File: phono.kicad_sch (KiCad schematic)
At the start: 63 parts, among them J1 Power +30V, J2 R Phono in, J3 L Phono in, J4 R Phono out, J5 L Phono out, Q1 2N2222, Q2 2N2222, Q3 2N2222, Q4 2N2222, Q5 2N2222, Q6 2N2222

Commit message: Add files via upload
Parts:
- removed C1, C11, C12, C13, C14, C15, C16, C17, C2, C4, C8, C9: 150uf, Capacitor_THT:CP_Radial_D10.0mm_P5.00mm, symbol Device:C_Polarized
- removed C10, C5: 47uf, Capacitor_THT:CP_Radial_D6.3mm_P2.50mm, symbol Device:C_Polarized
- removed C18, C6: 15uf, Capacitor_THT:CP_Radial_D5.0mm_P2.00mm, symbol Device:C_Polarized
- removed C19, C21: 6.8nf, Capacitor_THT:C_Rect_L7.0mm_W2.0mm_P5.00mm, symbol Device:C
- removed C20, C22: 22nf, Capacitor_THT:C_Rect_L7.0mm_W2.0mm_P5.00mm, symbol Device:C
- removed C3, C7: 1uf, Capacitor_THT:CP_Radial_D4.0mm_P2.00mm, symbol Device:C_Polarized
- removed D1, D2: 1N5250B, Diode_THT:D_DO-41_SOD81_P10.16mm_Horizontal, symbol Diode:1N47xxA
- removed J1: Power +30V, Connector_Wire:SolderWire-2sqmm_1x02_P7.8mm_D2mm_OD3.9mm, symbol Connector:Conn_01x02_Pin
- removed J2: R Phono in, Connector_Wire:SolderWire-2sqmm_1x01_D2mm_OD3.9mm, symbol Connector:Conn_01x01_Pin
- removed J3: L Phono in, Connector_Wire:SolderWire-2sqmm_1x01_D2mm_OD3.9mm, symbol Connector:Conn_01x01_Pin
- removed J4: R Phono out, Connector_Wire:SolderWire-2sqmm_1x01_D2mm_OD3.9mm, symbol Connector:Conn_01x01_Pin
- removed J5: L Phono out, Connector_Wire:SolderWire-2sqmm_1x01_D2mm_OD3.9mm, symbol Connector:Conn_01x01_Pin
- removed Q1, Q2, Q3, Q4, Q5, Q6: 2N2222, Package_TO_SOT_THT:TO-18-3, symbol Transistor_BJT:BC107
- removed R1, R15, R25, R8: 100, Resistor_THT:R_Axial_DIN0207_L6.3mm_D2.5mm_P10.16mm_Horizontal, symbol Device:R
- removed R10, R22: 270k, Resistor_THT:R_Axial_DIN0207_L6.3mm_D2.5mm_P10.16mm_Horizontal, symbol Device:R
- removed R11, R24: 6k, Resistor_THT:R_Axial_DIN0207_L6.3mm_D2.5mm_P10.16mm_Horizontal, symbol Device:R
- removed R12, R23: 680, Resistor_THT:R_Axial_DIN0207_L6.3mm_D2.5mm_P10.16mm_Horizontal, symbol Device:R
- removed R13, R27: 4k7, Resistor_THT:R_Axial_DIN0207_L6.3mm_D2.5mm_P10.16mm_Horizontal, symbol Device:R
- removed R14, R28: 10k, Resistor_THT:R_Axial_DIN0207_L6.3mm_D2.5mm_P10.16mm_Horizontal, symbol Device:R
- removed R16, R2: 47k, Resistor_THT:R_Axial_DIN0207_L6.3mm_D2.5mm_P10.16mm_Horizontal, symbol Device:R
- removed R17, R6: 8k2, Resistor_THT:R_Axial_DIN0207_L6.3mm_D2.5mm_P10.16mm_Horizontal, symbol Device:R
- removed R18, R3: 150, Resistor_THT:R_Axial_DIN0207_L6.3mm_D2.5mm_P10.16mm_Horizontal, symbol Device:R
- removed R19, R26, R4, R7: 1k8, Resistor_THT:R_Axial_DIN0207_L6.3mm_D2.5mm_P10.16mm_Horizontal, symbol Device:R
- removed R20, R5: 1k, Resistor_THT:R_Axial_DIN0207_L6.3mm_D2.5mm_P10.16mm_Horizontal, symbol Device:R
- removed R21, R9: 12k, Resistor_THT:R_Axial_DIN0207_L6.3mm_D2.5mm_P10.16mm_Horizontal, symbol Device:R
- added C1, C101, C102, C2, C8, C9: 300u, Capacitor_THT:CP_Radial_D10.0mm_P5.00mm, symbol Device:C_Polarized_Small
- added C103, C3: 6n8, Capacitor_THT:C_Axial_L3.8mm_D2.6mm_P10.00mm_Horizontal, symbol Device:C
- added C104, C4: 22n, Capacitor_THT:C_Axial_L3.8mm_D2.6mm_P10.00mm_Horizontal, symbol Device:C
- added C105, C5, C7: 47u, Capacitor_THT:CP_Radial_D10.0mm_P5.00mm, symbol Device:C_Polarized_Small
- added C106, C6: 1uF, Capacitor_THT:C_Axial_L3.8mm_D2.6mm_P10.00mm_Horizontal, symbol Device:C
- added J1, J3: Conn_01x03_Pin, TerminalBlock:TerminalBlock_bornier-3_P5.08mm, symbol Connector:Conn_01x03_Pin
- added J2: Conn_01x02_Pin, TerminalBlock:TerminalBlock_bornier-2_P5.08mm, symbol Connector:Conn_01x02_Pin
- added Q1, Q101, Q102, Q103, Q2, Q3: 2N2222, Package_TO_SOT_THT:TO-39-3, symbol Transistor_BJT:2N2219
- added R1, R101: 150, Resistor_THT:R_Axial_DIN0207_L6.3mm_D2.5mm_P10.16mm_Horizontal, symbol Device:R_Small
- added R10, R11, R110: 1K, Resistor_THT:R_Axial_DIN0207_L6.3mm_D2.5mm_P10.16mm_Horizontal, symbol Device:R_Small
- added R102, R109, R2, R9: 1K8, Resistor_THT:R_Axial_DIN0207_L6.3mm_D2.5mm_P10.16mm_Horizontal, symbol Device:R_Small
- added R103, R3: 8K2, Resistor_THT:R_Axial_DIN0207_L6.3mm_D2.5mm_P10.16mm_Horizontal, symbol Device:R_Small
- added R104, R108, R4, R8: 100, Resistor_THT:R_Axial_DIN0207_L6.3mm_D2.5mm_P10.16mm_Horizontal, symbol Device:R_Small
- added R105, R5: 12K, Resistor_THT:R_Axial_DIN0207_L6.3mm_D2.5mm_P10.16mm_Horizontal, symbol Device:R_Small
- added R106, R6: 270K, Resistor_THT:R_Axial_DIN0207_L6.3mm_D2.5mm_P10.16mm_Horizontal, symbol Device:R_Small
- added R107, R7: 6K, Resistor_THT:R_Axial_DIN0207_L6.3mm_D2.5mm_P10.16mm_Horizontal, symbol Device:R_Small
- added R112, R12: 47K, Resistor_THT:R_Axial_DIN0207_L6.3mm_D2.5mm_P10.16mm_Horizontal, symbol Device:R_Small
- added R113, R13: 4K7, Resistor_THT:R_Axial_DIN0207_L6.3mm_D2.5mm_P10.16mm_Horizontal, symbol Device:R_Small
- added R114, R14: 10K, Resistor_THT:R_Axial_DIN0207_L6.3mm_D2.5mm_P10.16mm_Horizontal, symbol Device:R_Small
- added R15: 15K, Resistor_THT:R_Axial_DIN0207_L6.3mm_D2.5mm_P10.16mm_Horizontal, symbol Device:R_Small
- added U1: LM317_TO-220, Package_TO_SOT_THT:TO-220-3_Vertical, symbol Regulator_Linear:LM317_TO-220
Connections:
- net +28V: now also J2.1 (Pin_1), Q103.3 (C), Q3.3 (C), R107.1, R7.2, U1.3 (VI)
- net GND: now also C1.2, C101.2, C102.2, C2.2, C7.2, C8.2, C9.2, J1.2 (Pin_2), J2.2 (Pin_2), J3.2 (Pin_2), R102.2, R109.2, R113.2, R114.2, R13.2, R14.2, R15.2, R2.2, R9.2
- new net: C106.2, R104.1
- new net: Q101.2 (B), R104.2, R112.1
- new net: C1.1, R1.2, R2.1
- new net: Q2.1 (E), R8.1
- new net: Q1.3 (C), Q2.2 (B), R3.2
- new net: C4.2, Q2.3 (C), Q3.2 (B), R6.2, R7.1
- new net: R11.2, R15.1, U1.1 (ADJ)
- new net: C2.1, R10.1, R12.2
- new net: C8.1, R10.2, R8.2, R9.1
- new net: C3.1, Q1.1 (E), R1.1, R5.1
- new net: C3.2, C4.1, R5.2, R6.1
- new net: C103.2, C104.1, R105.2, R106.1
- new net: C104.2, Q102.3 (C), Q103.2 (B), R106.2, R107.2
- new net: C105.1, Q103.1 (E), R113.1
- new net: C5.1, Q3.1 (E), R13.1
- new net: C6.2, R4.1
- new net: C103.1, Q101.1 (E), R101.1, R105.1
- new net: Q101.3 (C), Q102.2 (B), R103.2
- new net: C101.1, R101.2, R102.1
- new net: Q1.2 (B), R12.1, R4.2
- new net: C102.1, R110.1, R112.2
- new net: C9.1, R108.2, R109.1, R110.2
- new net: Q102.1 (E), R108.1
- new net +20V: C7.1, R103.1, R11.1, R3.1, U1.2 (VO)
- new net Input-L: C106.1, J1.3 (Pin_3)
- new net Input-R: C6.1, J1.1 (Pin_1)
- new net Output-L: C105.2, J3.3 (Pin_3), R114.1
- new net Output-R: C5.2, J3.1 (Pin_1), R14.1

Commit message: Add files via upload
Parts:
- added C10: 10u, Capacitor_THT:CP_Radial_D5.0mm_P2.00mm, symbol Device:C_Polarized_Small
- R11: value 1K -> 220
- R15: value 15K -> 3K3
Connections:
- net GND: now also C10.2
- net at R11.2, R15.1, U1.1 (ADJ): now also C10.1
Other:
- moved on the sheet: R15

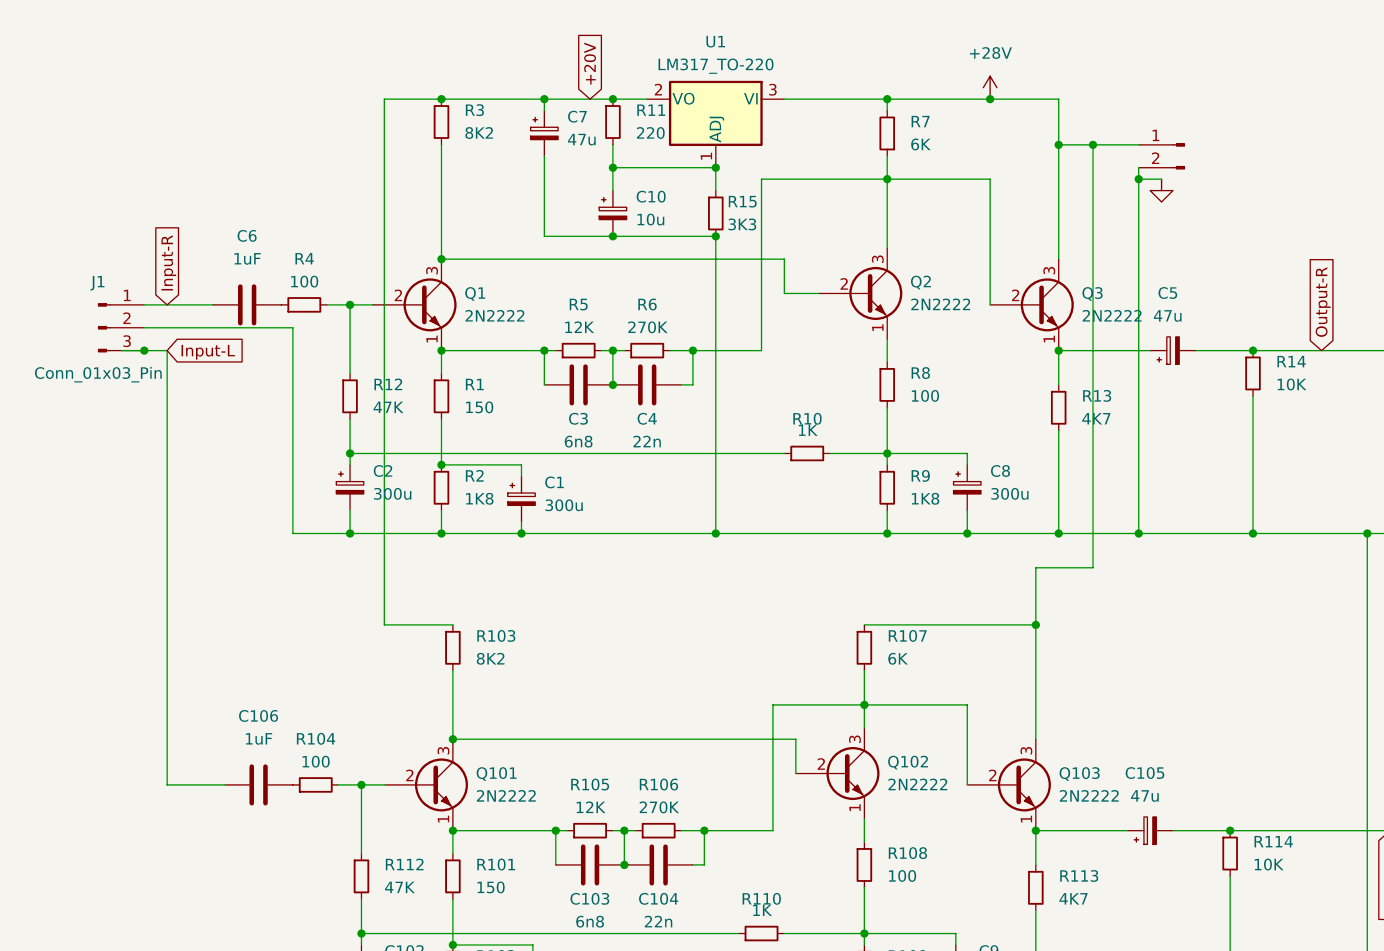
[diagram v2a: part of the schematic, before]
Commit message: Add files via upload
Esquema y placa actualizados para uso con Kicad 8
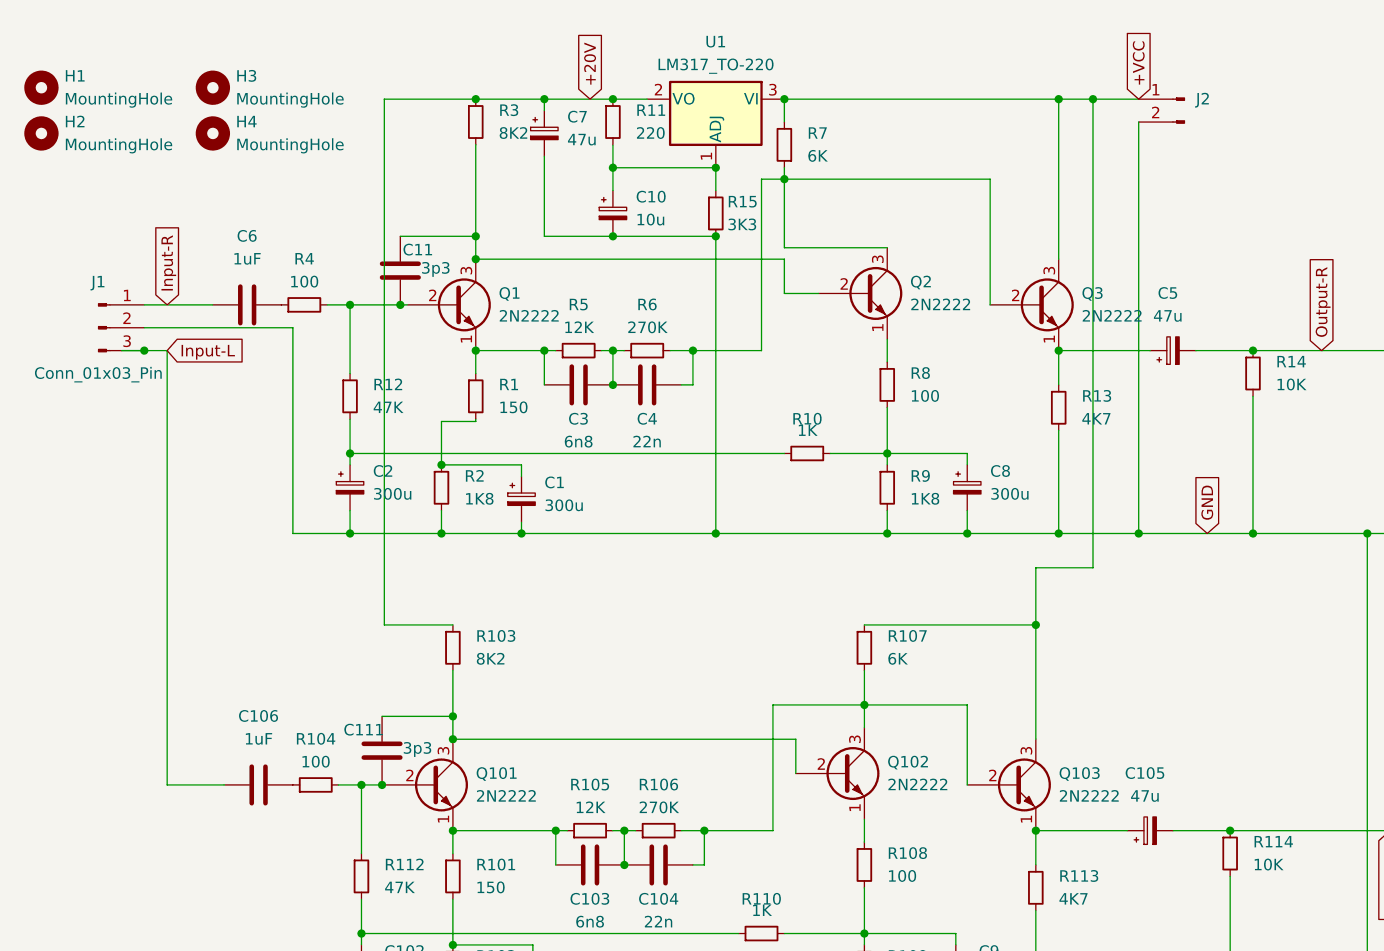
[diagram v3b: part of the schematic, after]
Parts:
- added C11, C111: 3p3, Capacitor_THT:C_Disc_D3.0mm_W2.0mm_P2.50mm, symbol Device:C
- added H1, H2, H3, H4: MountingHole, MountingHole:MountingHole_3.2mm_M3, symbol Mechanical:MountingHole
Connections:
- net at Q101.2 (B), R104.2, R112.1: now also C111.2
- net at Q1.3 (C), Q2.2 (B), R3.2: now also C11.1
- net at Q101.3 (C), Q102.2 (B), R103.2: now also C111.1
- net at Q1.2 (B), R12.1, R4.2: now also C11.2
- net +28V renamed +VCC
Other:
- moved on the sheet: Q1, R1, R3, R7
